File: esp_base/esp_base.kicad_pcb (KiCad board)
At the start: 2 copper layers, 35.5 x 45 mm, 52 parts, among them J1 Conn_01x02_Pin, J2 Conn_01x02_Pin, J3 Conn_01x02_Pin, U1 ESP32-C3-WROOM-02, U2 AP2112K-3.3

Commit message: added ground
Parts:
- added ?: , , F.Cu at (79.3, 91.0)
- added ?: , , F.Cu at (76.8, 91.0)
- added ?: , , F.Cu at (74.3, 91.0)
- added ?: , , F.Cu at (81.8, 91.0)
- added ?: , , F.Cu at (84.3, 91.0)
- renumbered 5V1 to 5V, GND1 to GND
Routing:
- net +3V3_UP: track 130.9 -> 134.9 mm
- net /F6: track 47.6 -> 50.7 mm
- net /F12: track 49.2 -> 49.9 mm
- net GND: vias 76 -> 75
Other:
- board text added: "GND"

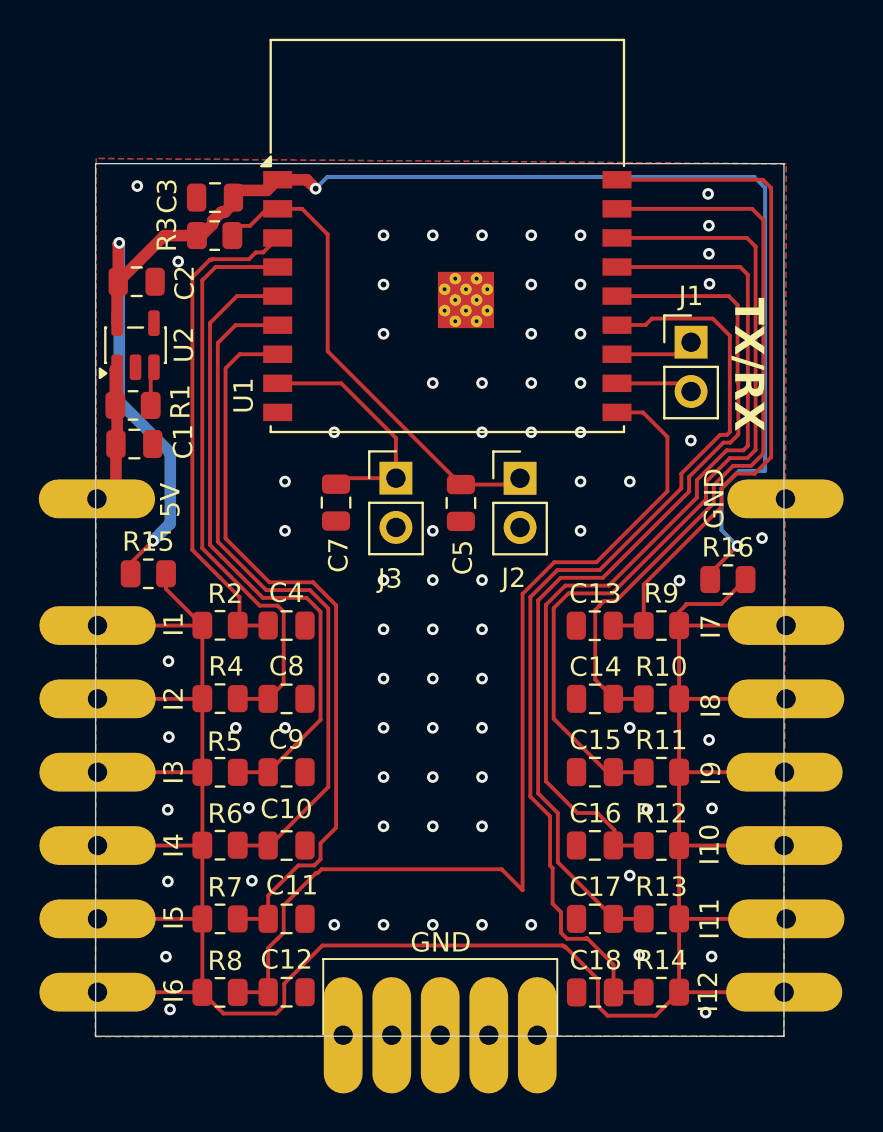
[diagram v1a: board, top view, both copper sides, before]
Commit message: komponent moved to new position smaller eddition
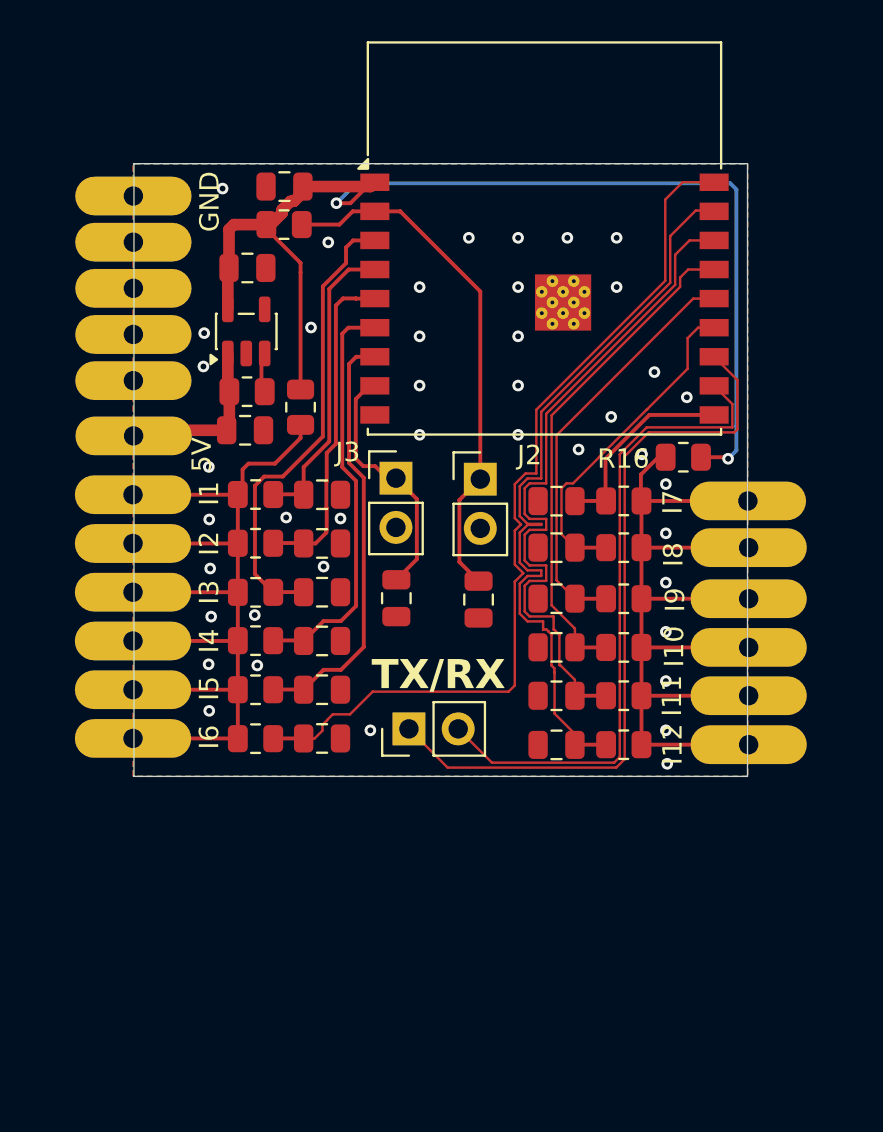
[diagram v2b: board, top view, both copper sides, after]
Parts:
- removed the ? at (79.3, 91.0)
- removed the ? at (76.8, 91.0)
- removed the ? at (74.3, 91.0)
- removed the ? at (81.8, 91.0)
- removed the ? at (84.3, 91.0)
- added ?: , , F.Cu at (63.5, 57.2)
- added ?: , , F.Cu at (63.5, 54.8)
- added ?: , , F.Cu at (63.5, 52.4)
- added ?: , , F.Cu at (63.5, 50.0)
- moved GND1 37.1 mm to (63.5, 47.7)
- moved J1 24.7 mm to (77.7, 75.2), turned to 90 degrees
- moved C12 13.2 mm to (73.2, 75.6)
- moved I6 13.2 mm to (63.4, 75.6)
- moved R8 13.2 mm to (69.7, 75.7)
- moved C18 12.9 mm to (85.3, 76.0)
- moved R14 12.9 mm to (88.7, 76.0)
- moved I12 12.9 mm to (95.2, 76.0)
- moved C11 12.0 mm to (73.2, 73.1)
- moved I5 12.0 mm to (63.4, 73.1)
- moved R7 12.0 mm to (69.7, 73.1)
- moved C17 11.7 mm to (85.3, 73.4)
- moved R13 11.7 mm to (88.7, 73.4)
- moved I11 11.7 mm to (95.2, 73.4)
- moved R15 11.6 mm to (72.1, 58.6), turned to -90 degrees
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- renumbered GND to GND1
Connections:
- U1 pad 10: /F6 -> /F7
- U1 pad 13: /F12 -> /F8
- U1 pad 14: /F11 -> /F9
- U1 pad 16: /F9 -> /F11
- U1 pad 17: /F8 -> /F12
- U1 pad 18: /F7 -> /F6
- U1 pad 3: /F1 -> /F3
- U1 pad 4: /F2 -> /F1
- U1 pad 5: /F3 -> /F2
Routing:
- net +3V3_UP: track 134.9 -> 92.9 mm
- net /TX: track 4.08 -> 38.4 mm
- net /RX: track 3.99 -> 33.7 mm
- net /F7: track 35.5 -> 10.3 mm
- net /F9: track 43.6 -> 21.4 mm
- net /F8: track 38.9 -> 17.1 mm
- net +3V3: track 82.6 -> 61.3 mm, vias 4 -> 2
- net /F10: track 46.1 -> 25.8 mm
- net /F5: track 38.5 -> 22.0 mm
- net /F4: track 35.9 -> 21.2 mm
- net /F2: track 29.8 -> 17.1 mm
- net /F11: track 47.0 -> 36.0 mm
- net /F12: track 49.9 -> 39.5 mm
- net /F1: track 25.8 -> 15.5 mm
- net /F3: track 33.5 -> 23.9 mm
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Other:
- board size 35.5 x 45 mm -> 31.6 x 31.6 mm

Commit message: NEW PADS
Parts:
- removed the 5V at (63.5, 60.0)
- removed the ? at (63.5, 57.2)
- removed the ? at (63.5, 54.8)
- removed the ? at (63.5, 52.4)
- removed the ? at (63.5, 50.0)
- removed GND1: TestPoint_Alt, TestPoint:TestPoint_THTPad_D2.0mm_Drill1.0mm
- added 5V: TestPoint_Alt, TestPoint:TestPoint_Pad_2.0x2.0mm, F.Cu at (64.8, 59.8)
- added ?: , , F.Cu at (65.3, 50.0)
- added ?: , , F.Cu at (65.3, 57.1)
- added ?: , , F.Cu at (65.3, 52.4)
- added GND: TestPoint_Alt, TestPoint:TestPoint_Pad_2.0x2.0mm, F.Cu at (65.3, 47.6)
- added GND: TestPoint_Alt, TestPoint:TestPoint_Pad_2.0x2.0mm, F.Cu at (65.3, 54.7)
- I1, I10, I11, I12, I2, I3, I4, I5, I6, I7, I8, I9: footprint TestPoint:TestPoint_THTPad_D2.0mm_Drill1.0mm -> TestPoint:TestPoint_Pad_2.0x2.0mm
- moved I7 12.8 mm to (92.7, 76.0), turned to 0 degrees
- moved I12 12.7 mm to (93.2, 63.4), turned to 0 degrees
- moved I8 7.90 mm to (93.2, 73.5), turned to 0 degrees
- moved I11 7.78 mm to (93.2, 65.9), turned to 0 degrees
- moved I10 3.35 mm to (93.2, 68.2), turned to 0 degrees
- moved I9 3.15 mm to (93.2, 70.9), turned to 0 degrees
- moved I5 1.84 mm to (65.3, 73.3), turned to 0 degrees
- moved I1 1.83 mm to (65.3, 63.0), turned to 0 degrees
- moved I4 1.83 mm to (65.3, 70.7), turned to 0 degrees
- moved I2 1.83 mm to (65.3, 65.5), turned to 0 degrees
- moved I6 1.83 mm to (65.3, 75.7), turned to 0 degrees
- moved I3 1.83 mm to (65.3, 68.1), turned to 0 degrees
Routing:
- net GND: vias 42 -> 40

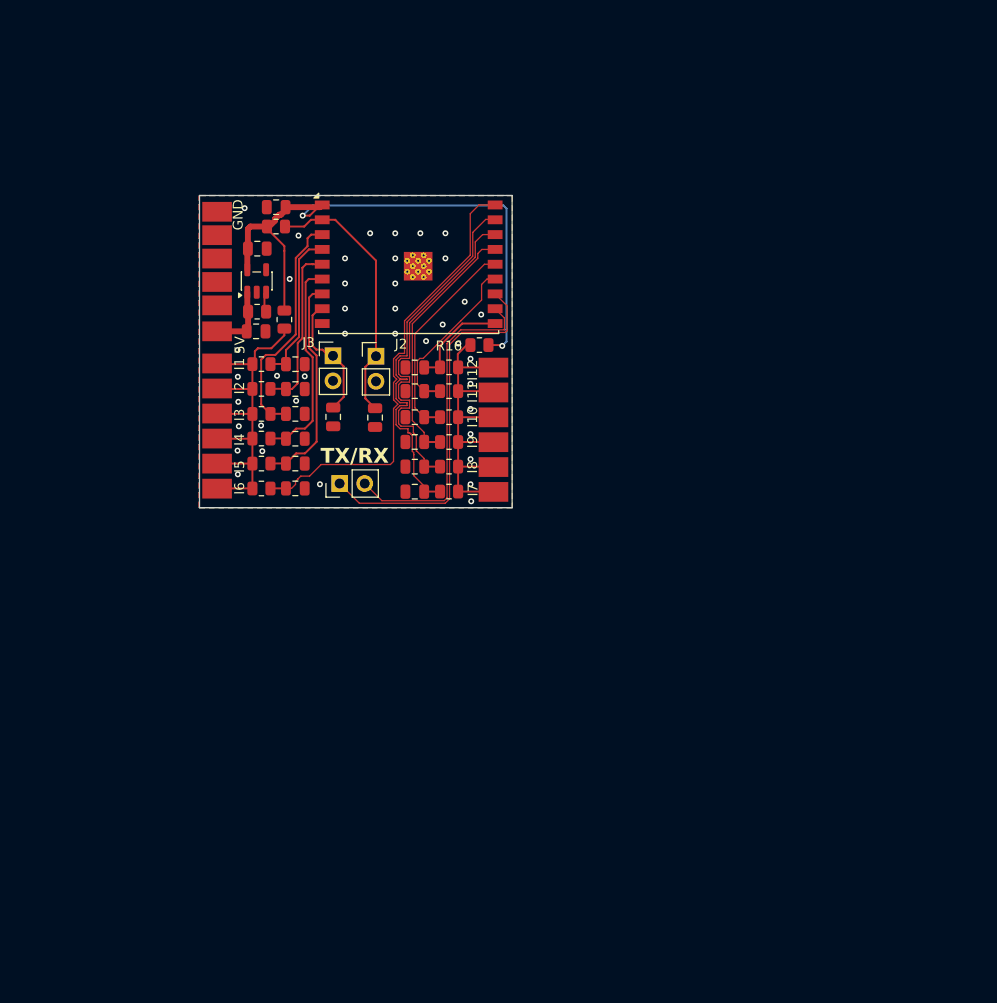
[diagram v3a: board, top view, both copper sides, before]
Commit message: last version with cahges on pull up resistor
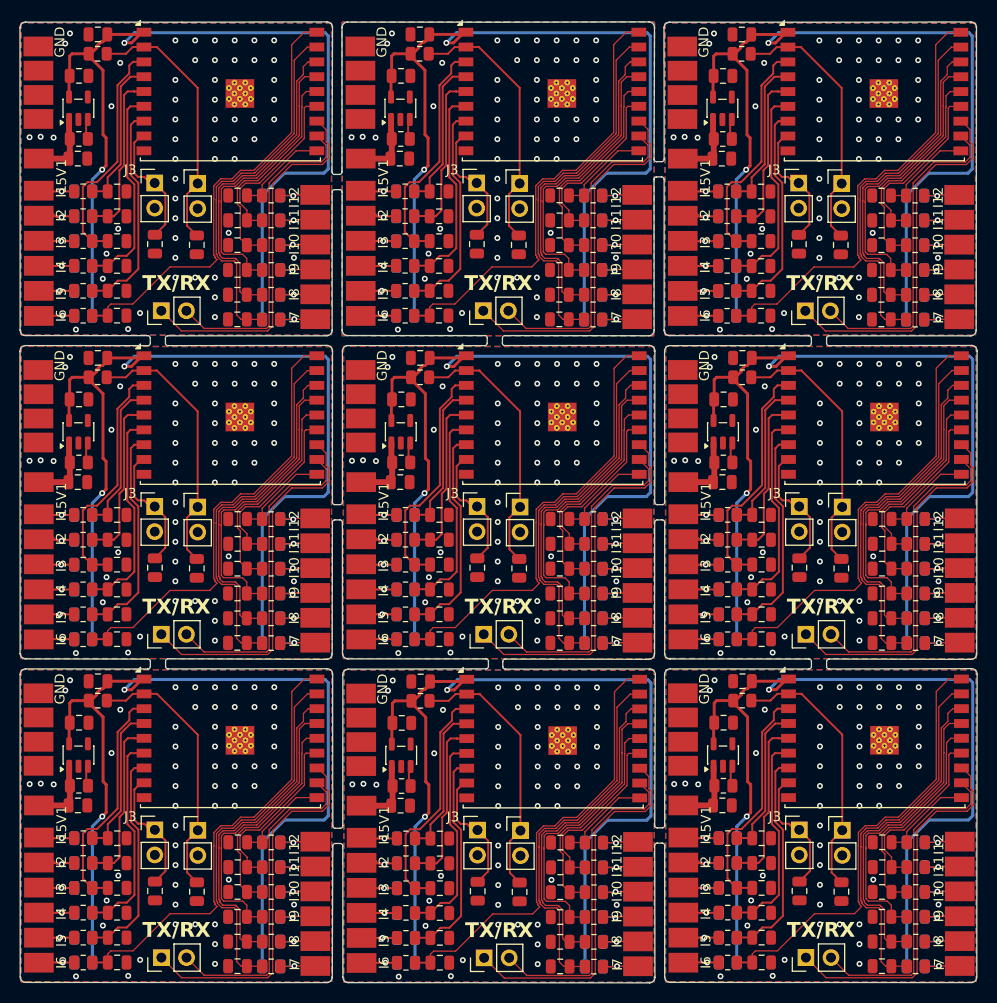
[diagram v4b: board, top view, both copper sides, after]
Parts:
- removed the ? at (65.3, 50.0)
- removed the ? at (65.3, 57.1)
- removed the ? at (65.3, 52.4)
- removed GND: TestPoint_Alt, TestPoint:TestPoint_Pad_2.0x2.0mm
- removed R15, R16: 4k7, Resistor_SMD:R_0805_2012Metric
- added 5V1: TestPoint_Alt, TestPoint:TestPoint_Pad_2.0x2.0mm, F.Cu at (111.9, 42.3)
- added 5V1: TestPoint_Alt, TestPoint:TestPoint_Pad_2.0x2.0mm, F.Cu at (111.9, 75.0)
- added 5V1: TestPoint_Alt, TestPoint:TestPoint_Pad_2.0x2.0mm, F.Cu at (79.3, 42.3)
- added 5V1: TestPoint_Alt, TestPoint:TestPoint_Pad_2.0x2.0mm, F.Cu at (46.7, 107.7)
- added 5V1: TestPoint_Alt, TestPoint:TestPoint_Pad_2.0x2.0mm, F.Cu at (46.7, 75.0)
- added 5V1: TestPoint_Alt, TestPoint:TestPoint_Pad_2.0x2.0mm, F.Cu at (112.0, 107.7)
- added 5V1: TestPoint_Alt, TestPoint:TestPoint_Pad_2.0x2.0mm, F.Cu at (79.3, 75.0)
- added 5V1: TestPoint_Alt, TestPoint:TestPoint_Pad_2.0x2.0mm, F.Cu at (79.4, 107.8)
- added ?: , , F.Cu at (112.4, 71.0)
- added ?: , , F.Cu at (79.8, 38.3)
- added ?: , , F.Cu at (79.8, 35.8)
- added ?: , , F.Cu at (79.8, 71.0)
- added ?: , , F.Cu at (47.2, 66.1)
- added ?: , , F.Cu at (112.4, 101.3)
- added ?: , , F.Cu at (47.2, 38.3)
- added ?: , , F.Cu at (79.9, 98.9)
- added ?: , , F.Cu at (79.9, 101.3)
- added ?: , , F.Cu at (47.2, 33.4)
- added ?: , , F.Cu at (79.8, 68.6)
- added ?: , , F.Cu at (112.4, 38.3)
- added ?: , , F.Cu at (112.4, 66.1)
- added ?: , , F.Cu at (47.2, 101.3)
- added ?: , , F.Cu at (79.9, 103.7)
- added ?: , , F.Cu at (47.2, 68.6)
- added ?: , , F.Cu at (112.4, 68.6)
- added ?: , , F.Cu at (112.4, 98.8)
- added ?: , , F.Cu at (79.8, 33.4)
- added ?: , , F.Cu at (79.8, 66.1)
- added ?: , , F.Cu at (112.4, 103.7)
- added ?: , , F.Cu at (112.4, 33.4)
- added ?: , , F.Cu at (47.2, 103.7)
- added ?: , , F.Cu at (47.2, 35.8)
- added ?: , , F.Cu at (47.2, 71.0)
- added ?: , , F.Cu at (47.2, 98.8)
- added ?: , , F.Cu at (112.4, 35.8)
- added C1: 1u, Capacitor_SMD:C_0805_2012Metric, F.Cu at (116.4, 75.0)
- added C1: 1u, Capacitor_SMD:C_0805_2012Metric, F.Cu at (51.2, 107.7)
- added C1: 1u, Capacitor_SMD:C_0805_2012Metric, F.Cu at (116.3, 42.3)
- added C1: 1u, Capacitor_SMD:C_0805_2012Metric, F.Cu at (83.8, 42.3)
- added C1: 1u, Capacitor_SMD:C_0805_2012Metric, F.Cu at (116.4, 107.7)
- added C1: 1u, Capacitor_SMD:C_0805_2012Metric, F.Cu at (51.2, 75.0)
- added C1: 1u, Capacitor_SMD:C_0805_2012Metric, F.Cu at (83.8, 107.8)
- added C1: 1u, Capacitor_SMD:C_0805_2012Metric, F.Cu at (83.8, 75.0)
- added C10: 4u7, Capacitor_SMD:C_0805_2012Metric, F.Cu at (87.7, 53.1)
- added C10: 4u7, Capacitor_SMD:C_0805_2012Metric, F.Cu at (120.4, 85.9)
- added C10: 4u7, Capacitor_SMD:C_0805_2012Metric, F.Cu at (87.8, 85.9)
- added C10: 4u7, Capacitor_SMD:C_0805_2012Metric, F.Cu at (87.8, 118.6)
- added C10: 4u7, Capacitor_SMD:C_0805_2012Metric, F.Cu at (120.3, 53.1)
- added C10: 4u7, Capacitor_SMD:C_0805_2012Metric, F.Cu at (55.1, 118.6)
- added C10: 4u7, Capacitor_SMD:C_0805_2012Metric, F.Cu at (55.1, 85.9)
- added C10: 4u7, Capacitor_SMD:C_0805_2012Metric, F.Cu at (120.4, 118.6)
- added C11: 4u7, Capacitor_SMD:C_0805_2012Metric, F.Cu at (120.3, 55.7)
- added C11: 4u7, Capacitor_SMD:C_0805_2012Metric, F.Cu at (87.8, 121.1)
- added C11: 4u7, Capacitor_SMD:C_0805_2012Metric, F.Cu at (120.4, 121.1)
- added C11: 4u7, Capacitor_SMD:C_0805_2012Metric, F.Cu at (87.8, 88.4)
- added C11: 4u7, Capacitor_SMD:C_0805_2012Metric, F.Cu at (120.4, 88.4)
- added C11: 4u7, Capacitor_SMD:C_0805_2012Metric, F.Cu at (55.1, 121.1)
- added C11: 4u7, Capacitor_SMD:C_0805_2012Metric, F.Cu at (87.7, 55.6)
- added C11: 4u7, Capacitor_SMD:C_0805_2012Metric, F.Cu at (55.1, 88.4)
- added C12: 4u7, Capacitor_SMD:C_0805_2012Metric, F.Cu at (55.1, 123.6)
- added C12: 4u7, Capacitor_SMD:C_0805_2012Metric, F.Cu at (87.8, 90.9)
- added C12: 4u7, Capacitor_SMD:C_0805_2012Metric, F.Cu at (87.7, 58.2)
- added C12: 4u7, Capacitor_SMD:C_0805_2012Metric, F.Cu at (120.3, 58.2)
- added C12: 4u7, Capacitor_SMD:C_0805_2012Metric, F.Cu at (120.4, 90.9)
- added C12: 4u7, Capacitor_SMD:C_0805_2012Metric, F.Cu at (87.8, 123.6)
- added C12: 4u7, Capacitor_SMD:C_0805_2012Metric, F.Cu at (55.1, 90.9)
- added C12: 4u7, Capacitor_SMD:C_0805_2012Metric, F.Cu at (120.4, 123.6)
- added C13: 4u7, Capacitor_SMD:C_0805_2012Metric, F.Cu at (132.5, 124.0)
- added C13: 4u7, Capacitor_SMD:C_0805_2012Metric, F.Cu at (100.0, 124.0)
- added C13: 4u7, Capacitor_SMD:C_0805_2012Metric, F.Cu at (99.9, 91.3)
- added C13: 4u7, Capacitor_SMD:C_0805_2012Metric, F.Cu at (67.3, 124.0)
- added C13: 4u7, Capacitor_SMD:C_0805_2012Metric, F.Cu at (132.5, 91.3)
- added C13: 4u7, Capacitor_SMD:C_0805_2012Metric, F.Cu at (99.9, 58.5)
- added C13: 4u7, Capacitor_SMD:C_0805_2012Metric, F.Cu at (67.3, 91.3)
- added C13: 4u7, Capacitor_SMD:C_0805_2012Metric, F.Cu at (132.5, 58.5)
- added C14: 4u7, Capacitor_SMD:C_0805_2012Metric, F.Cu at (67.3, 121.5)
- added C14: 4u7, Capacitor_SMD:C_0805_2012Metric, F.Cu at (132.5, 56.1)
- added C14: 4u7, Capacitor_SMD:C_0805_2012Metric, F.Cu at (99.9, 56.0)
- added C14: 4u7, Capacitor_SMD:C_0805_2012Metric, F.Cu at (132.5, 121.5)
- added C14: 4u7, Capacitor_SMD:C_0805_2012Metric, F.Cu at (99.9, 88.8)
- added C14: 4u7, Capacitor_SMD:C_0805_2012Metric, F.Cu at (67.3, 88.8)
- added C14: 4u7, Capacitor_SMD:C_0805_2012Metric, F.Cu at (100.0, 121.5)
- added C14: 4u7, Capacitor_SMD:C_0805_2012Metric, F.Cu at (132.5, 88.8)
- added C15: 4u7, Capacitor_SMD:C_0805_2012Metric, F.Cu at (100.0, 119.0)
- added C15: 4u7, Capacitor_SMD:C_0805_2012Metric, F.Cu at (67.3, 86.3)
- added C15: 4u7, Capacitor_SMD:C_0805_2012Metric, F.Cu at (132.5, 86.3)
- added C15: 4u7, Capacitor_SMD:C_0805_2012Metric, F.Cu at (99.9, 86.3)
- added C15: 4u7, Capacitor_SMD:C_0805_2012Metric, F.Cu at (67.3, 119.0)
- added C15: 4u7, Capacitor_SMD:C_0805_2012Metric, F.Cu at (99.9, 53.5)
- added C15: 4u7, Capacitor_SMD:C_0805_2012Metric, F.Cu at (132.5, 119.0)
- added C15: 4u7, Capacitor_SMD:C_0805_2012Metric, F.Cu at (132.5, 53.5)
- added C16: 4u7, Capacitor_SMD:C_0805_2012Metric, F.Cu at (100.0, 83.8)
- added C16: 4u7, Capacitor_SMD:C_0805_2012Metric, F.Cu at (67.3, 116.5)
- added C16: 4u7, Capacitor_SMD:C_0805_2012Metric, F.Cu at (100.0, 116.5)
- added C16: 4u7, Capacitor_SMD:C_0805_2012Metric, F.Cu at (99.9, 51.0)
- added C16: 4u7, Capacitor_SMD:C_0805_2012Metric, F.Cu at (132.5, 51.0)
- added C16: 4u7, Capacitor_SMD:C_0805_2012Metric, F.Cu at (132.6, 83.8)
- added C16: 4u7, Capacitor_SMD:C_0805_2012Metric, F.Cu at (67.3, 83.8)
- added C16: 4u7, Capacitor_SMD:C_0805_2012Metric, F.Cu at (132.6, 116.5)
- added C17: 4u7, Capacitor_SMD:C_0805_2012Metric, F.Cu at (132.5, 48.5)
- added C17: 4u7, Capacitor_SMD:C_0805_2012Metric, F.Cu at (132.6, 114.0)
- added C17: 4u7, Capacitor_SMD:C_0805_2012Metric, F.Cu at (99.9, 48.5)
- added C17: 4u7, Capacitor_SMD:C_0805_2012Metric, F.Cu at (100.0, 81.3)
- added C17: 4u7, Capacitor_SMD:C_0805_2012Metric, F.Cu at (100.0, 114.0)
- added C17: 4u7, Capacitor_SMD:C_0805_2012Metric, F.Cu at (67.3, 114.0)
- added C17: 4u7, Capacitor_SMD:C_0805_2012Metric, F.Cu at (67.3, 81.3)
- added C17: 4u7, Capacitor_SMD:C_0805_2012Metric, F.Cu at (132.6, 81.3)
- added C18: 4u7, Capacitor_SMD:C_0805_2012Metric, F.Cu at (132.6, 111.5)
- added C18: 4u7, Capacitor_SMD:C_0805_2012Metric, F.Cu at (132.6, 78.7)
- added C18: 4u7, Capacitor_SMD:C_0805_2012Metric, F.Cu at (67.3, 78.7)
- added C18: 4u7, Capacitor_SMD:C_0805_2012Metric, F.Cu at (132.5, 46.0)
- added C18: 4u7, Capacitor_SMD:C_0805_2012Metric, F.Cu at (100.0, 78.7)
- added C18: 4u7, Capacitor_SMD:C_0805_2012Metric, F.Cu at (99.9, 46.0)
- added C18: 4u7, Capacitor_SMD:C_0805_2012Metric, F.Cu at (100.0, 111.5)
- added C18: 4u7, Capacitor_SMD:C_0805_2012Metric, F.Cu at (67.3, 111.5)
- added C2: 1u, Capacitor_SMD:C_0805_2012Metric, F.Cu at (116.5, 99.4)
- added C2: 1u, Capacitor_SMD:C_0805_2012Metric, F.Cu at (84.0, 99.4)
- added C2: 1u, Capacitor_SMD:C_0805_2012Metric, F.Cu at (116.5, 33.9)
- added C2: 1u, Capacitor_SMD:C_0805_2012Metric, F.Cu at (83.9, 33.9)
- added C2: 1u, Capacitor_SMD:C_0805_2012Metric, F.Cu at (116.5, 66.6)
- added C2: 1u, Capacitor_SMD:C_0805_2012Metric, F.Cu at (83.9, 66.6)
- added C2: 1u, Capacitor_SMD:C_0805_2012Metric, F.Cu at (51.3, 66.6)
- added C2: 1u, Capacitor_SMD:C_0805_2012Metric, F.Cu at (51.3, 99.4)
- added C3: 1u, Capacitor_SMD:C_0805_2012Metric, F.Cu at (118.4, 29.7)
- added C3: 1u, Capacitor_SMD:C_0805_2012Metric, F.Cu at (53.2, 95.2)
- added C3: 1u, Capacitor_SMD:C_0805_2012Metric, F.Cu at (85.9, 95.2)
- added C3: 1u, Capacitor_SMD:C_0805_2012Metric, F.Cu at (85.8, 29.7)
- added C3: 1u, Capacitor_SMD:C_0805_2012Metric, F.Cu at (85.8, 62.4)
- added C3: 1u, Capacitor_SMD:C_0805_2012Metric, F.Cu at (118.4, 62.4)
- added C3: 1u, Capacitor_SMD:C_0805_2012Metric, F.Cu at (118.4, 95.2)
- added C3: 1u, Capacitor_SMD:C_0805_2012Metric, F.Cu at (53.2, 62.4)
- added C4: 4u7, Capacitor_SMD:C_0805_2012Metric, F.Cu at (87.8, 78.3)
- added C4: 4u7, Capacitor_SMD:C_0805_2012Metric, F.Cu at (55.1, 78.3)
- added C4: 4u7, Capacitor_SMD:C_0805_2012Metric, F.Cu at (55.1, 111.1)
- added C4: 4u7, Capacitor_SMD:C_0805_2012Metric, F.Cu at (120.4, 111.0)
- added C4: 4u7, Capacitor_SMD:C_0805_2012Metric, F.Cu at (87.8, 111.1)
- added C4: 4u7, Capacitor_SMD:C_0805_2012Metric, F.Cu at (120.4, 78.3)
- added C4: 4u7, Capacitor_SMD:C_0805_2012Metric, F.Cu at (120.3, 45.6)
- added C4: 4u7, Capacitor_SMD:C_0805_2012Metric, F.Cu at (87.7, 45.6)
- added C5: 1u, Capacitor_SMD:C_0805_2012Metric, F.Cu at (95.9, 116.5)
- added C5: 1u, Capacitor_SMD:C_0805_2012Metric, F.Cu at (63.2, 83.7)
- added C5: 1u, Capacitor_SMD:C_0805_2012Metric, F.Cu at (128.4, 83.7)
- added C5: 1u, Capacitor_SMD:C_0805_2012Metric, F.Cu at (63.2, 116.5)
- added C5: 1u, Capacitor_SMD:C_0805_2012Metric, F.Cu at (95.8, 83.7)
- added C5: 1u, Capacitor_SMD:C_0805_2012Metric, F.Cu at (128.4, 116.5)
- added C5: 1u, Capacitor_SMD:C_0805_2012Metric, F.Cu at (128.4, 51.0)
- added C5: 1u, Capacitor_SMD:C_0805_2012Metric, F.Cu at (95.8, 51.0)
- added C7: 1u, Capacitor_SMD:C_0805_2012Metric, F.Cu at (124.1, 50.9)
- added C7: 1u, Capacitor_SMD:C_0805_2012Metric, F.Cu at (124.2, 116.4)
- added C7: 1u, Capacitor_SMD:C_0805_2012Metric, F.Cu at (59.0, 116.4)
- added C7: 1u, Capacitor_SMD:C_0805_2012Metric, F.Cu at (59.0, 83.7)
- added C7: 1u, Capacitor_SMD:C_0805_2012Metric, F.Cu at (91.6, 116.4)
- added C7: 1u, Capacitor_SMD:C_0805_2012Metric, F.Cu at (91.6, 83.7)
- added C7: 1u, Capacitor_SMD:C_0805_2012Metric, F.Cu at (91.6, 50.9)
- added C7: 1u, Capacitor_SMD:C_0805_2012Metric, F.Cu at (124.2, 83.7)
- added C8: 4u7, Capacitor_SMD:C_0805_2012Metric, F.Cu at (55.1, 80.8)
- added C8: 4u7, Capacitor_SMD:C_0805_2012Metric, F.Cu at (87.7, 48.1)
- added C8: 4u7, Capacitor_SMD:C_0805_2012Metric, F.Cu at (87.8, 113.6)
- added C8: 4u7, Capacitor_SMD:C_0805_2012Metric, F.Cu at (120.4, 113.6)
- added C8: 4u7, Capacitor_SMD:C_0805_2012Metric, F.Cu at (55.1, 113.6)
- added C8: 4u7, Capacitor_SMD:C_0805_2012Metric, F.Cu at (120.3, 48.1)
- added C8: 4u7, Capacitor_SMD:C_0805_2012Metric, F.Cu at (87.8, 80.8)
- added C8: 4u7, Capacitor_SMD:C_0805_2012Metric, F.Cu at (120.4, 80.8)
- added C9: 4u7, Capacitor_SMD:C_0805_2012Metric, F.Cu at (120.3, 50.6)
- added C9: 4u7, Capacitor_SMD:C_0805_2012Metric, F.Cu at (55.1, 83.4)
- added C9: 4u7, Capacitor_SMD:C_0805_2012Metric, F.Cu at (87.7, 50.6)
- added C9: 4u7, Capacitor_SMD:C_0805_2012Metric, F.Cu at (120.4, 116.1)
- added C9: 4u7, Capacitor_SMD:C_0805_2012Metric, F.Cu at (87.8, 116.1)
- added C9: 4u7, Capacitor_SMD:C_0805_2012Metric, F.Cu at (120.4, 83.4)
- added C9: 4u7, Capacitor_SMD:C_0805_2012Metric, F.Cu at (87.8, 83.4)
- added C9: 4u7, Capacitor_SMD:C_0805_2012Metric, F.Cu at (55.1, 116.1)
- added GND1: TestPoint_Alt, TestPoint:TestPoint_Pad_2.0x2.0mm, F.Cu at (112.4, 63.7)
- added GND1: TestPoint_Alt, TestPoint:TestPoint_Pad_2.0x2.0mm, F.Cu at (47.2, 96.4)
- added GND1: TestPoint_Alt, TestPoint:TestPoint_Pad_2.0x2.0mm, F.Cu at (47.2, 63.7)
- added GND1: TestPoint_Alt, TestPoint:TestPoint_Pad_2.0x2.0mm, F.Cu at (112.3, 30.9)
- added GND1: TestPoint_Alt, TestPoint:TestPoint_Pad_2.0x2.0mm, F.Cu at (79.8, 63.7)
- added GND1: TestPoint_Alt, TestPoint:TestPoint_Pad_2.0x2.0mm, F.Cu at (112.4, 96.4)
- added GND1: TestPoint_Alt, TestPoint:TestPoint_Pad_2.0x2.0mm, F.Cu at (79.7, 30.9)
- added GND1: TestPoint_Alt, TestPoint:TestPoint_Pad_2.0x2.0mm, F.Cu at (79.8, 96.4)
- added I1: TestPoint_Alt, TestPoint:TestPoint_Pad_2.0x2.0mm, F.Cu at (79.8, 45.5)
- added I1: TestPoint_Alt, TestPoint:TestPoint_Pad_2.0x2.0mm, F.Cu at (112.4, 45.5)
- added I1: TestPoint_Alt, TestPoint:TestPoint_Pad_2.0x2.0mm, F.Cu at (112.5, 111.0)
- added I1: TestPoint_Alt, TestPoint:TestPoint_Pad_2.0x2.0mm, F.Cu at (112.4, 78.3)
- added I1: TestPoint_Alt, TestPoint:TestPoint_Pad_2.0x2.0mm, F.Cu at (79.9, 111.0)
- added I1: TestPoint_Alt, TestPoint:TestPoint_Pad_2.0x2.0mm, F.Cu at (47.2, 78.3)
- added I1: TestPoint_Alt, TestPoint:TestPoint_Pad_2.0x2.0mm, F.Cu at (79.8, 78.3)
- added I1: TestPoint_Alt, TestPoint:TestPoint_Pad_2.0x2.0mm, F.Cu at (47.2, 111.0)
- added I10: TestPoint_Alt, TestPoint:TestPoint_Pad_2.0x2.0mm, F.Cu at (107.8, 50.7)
- added I10: TestPoint_Alt, TestPoint:TestPoint_Pad_2.0x2.0mm, F.Cu at (107.9, 116.2)
- added I10: TestPoint_Alt, TestPoint:TestPoint_Pad_2.0x2.0mm, F.Cu at (107.8, 83.5)
- added I10: TestPoint_Alt, TestPoint:TestPoint_Pad_2.0x2.0mm, F.Cu at (140.4, 83.5)
- added I10: TestPoint_Alt, TestPoint:TestPoint_Pad_2.0x2.0mm, F.Cu at (140.4, 116.2)
- added I10: TestPoint_Alt, TestPoint:TestPoint_Pad_2.0x2.0mm, F.Cu at (140.4, 50.7)
- added I10: TestPoint_Alt, TestPoint:TestPoint_Pad_2.0x2.0mm, F.Cu at (75.2, 83.5)
- added I10: TestPoint_Alt, TestPoint:TestPoint_Pad_2.0x2.0mm, F.Cu at (75.2, 116.2)
- added I11: TestPoint_Alt, TestPoint:TestPoint_Pad_2.0x2.0mm, F.Cu at (107.8, 81.2)
- added I11: TestPoint_Alt, TestPoint:TestPoint_Pad_2.0x2.0mm, F.Cu at (140.4, 81.2)
- added I11: TestPoint_Alt, TestPoint:TestPoint_Pad_2.0x2.0mm, F.Cu at (107.9, 113.9)
- added I11: TestPoint_Alt, TestPoint:TestPoint_Pad_2.0x2.0mm, F.Cu at (107.8, 48.4)
- added I11: TestPoint_Alt, TestPoint:TestPoint_Pad_2.0x2.0mm, F.Cu at (75.2, 81.2)
- added I11: TestPoint_Alt, TestPoint:TestPoint_Pad_2.0x2.0mm, F.Cu at (140.4, 113.9)
- added I11: TestPoint_Alt, TestPoint:TestPoint_Pad_2.0x2.0mm, F.Cu at (75.2, 113.9)
- added I11: TestPoint_Alt, TestPoint:TestPoint_Pad_2.0x2.0mm, F.Cu at (140.4, 48.4)
- added I12: TestPoint_Alt, TestPoint:TestPoint_Pad_2.0x2.0mm, F.Cu at (107.8, 78.7)
- added I12: TestPoint_Alt, TestPoint:TestPoint_Pad_2.0x2.0mm, F.Cu at (75.2, 78.7)
- added I12: TestPoint_Alt, TestPoint:TestPoint_Pad_2.0x2.0mm, F.Cu at (140.4, 111.4)
- added I12: TestPoint_Alt, TestPoint:TestPoint_Pad_2.0x2.0mm, F.Cu at (140.4, 45.9)
- added I12: TestPoint_Alt, TestPoint:TestPoint_Pad_2.0x2.0mm, F.Cu at (107.9, 111.4)
- added I12: TestPoint_Alt, TestPoint:TestPoint_Pad_2.0x2.0mm, F.Cu at (107.8, 45.9)
- added I12: TestPoint_Alt, TestPoint:TestPoint_Pad_2.0x2.0mm, F.Cu at (140.4, 78.7)
- added I12: TestPoint_Alt, TestPoint:TestPoint_Pad_2.0x2.0mm, F.Cu at (75.2, 111.4)
- added I2: TestPoint_Alt, TestPoint:TestPoint_Pad_2.0x2.0mm, F.Cu at (112.4, 80.8)
- added I2: TestPoint_Alt, TestPoint:TestPoint_Pad_2.0x2.0mm, F.Cu at (47.2, 80.8)
- added I2: TestPoint_Alt, TestPoint:TestPoint_Pad_2.0x2.0mm, F.Cu at (112.4, 48.1)
- added I2: TestPoint_Alt, TestPoint:TestPoint_Pad_2.0x2.0mm, F.Cu at (79.8, 80.8)
- added I2: TestPoint_Alt, TestPoint:TestPoint_Pad_2.0x2.0mm, F.Cu at (79.9, 113.6)
- added I2: TestPoint_Alt, TestPoint:TestPoint_Pad_2.0x2.0mm, F.Cu at (47.2, 113.5)
- added I2: TestPoint_Alt, TestPoint:TestPoint_Pad_2.0x2.0mm, F.Cu at (112.5, 113.5)
- added I2: TestPoint_Alt, TestPoint:TestPoint_Pad_2.0x2.0mm, F.Cu at (79.8, 48.1)
- added I3: TestPoint_Alt, TestPoint:TestPoint_Pad_2.0x2.0mm, F.Cu at (79.8, 50.6)
- added I3: TestPoint_Alt, TestPoint:TestPoint_Pad_2.0x2.0mm, F.Cu at (112.4, 50.6)
- added I3: TestPoint_Alt, TestPoint:TestPoint_Pad_2.0x2.0mm, F.Cu at (112.4, 83.4)
- added I3: TestPoint_Alt, TestPoint:TestPoint_Pad_2.0x2.0mm, F.Cu at (112.5, 116.1)
- added I3: TestPoint_Alt, TestPoint:TestPoint_Pad_2.0x2.0mm, F.Cu at (79.8, 83.4)
- added I3: TestPoint_Alt, TestPoint:TestPoint_Pad_2.0x2.0mm, F.Cu at (47.2, 83.4)
- added I3: TestPoint_Alt, TestPoint:TestPoint_Pad_2.0x2.0mm, F.Cu at (47.2, 116.1)
- added I3: TestPoint_Alt, TestPoint:TestPoint_Pad_2.0x2.0mm, F.Cu at (79.9, 116.1)
- added I4: TestPoint_Alt, TestPoint:TestPoint_Pad_2.0x2.0mm, F.Cu at (79.8, 53.2)
- added I4: TestPoint_Alt, TestPoint:TestPoint_Pad_2.0x2.0mm, F.Cu at (47.2, 85.9)
- added I4: TestPoint_Alt, TestPoint:TestPoint_Pad_2.0x2.0mm, F.Cu at (112.4, 53.2)
- added I4: TestPoint_Alt, TestPoint:TestPoint_Pad_2.0x2.0mm, F.Cu at (112.4, 85.9)
- added I4: TestPoint_Alt, TestPoint:TestPoint_Pad_2.0x2.0mm, F.Cu at (79.8, 85.9)
- added I4: TestPoint_Alt, TestPoint:TestPoint_Pad_2.0x2.0mm, F.Cu at (47.2, 118.6)
- added I4: TestPoint_Alt, TestPoint:TestPoint_Pad_2.0x2.0mm, F.Cu at (112.5, 118.6)
- added I4: TestPoint_Alt, TestPoint:TestPoint_Pad_2.0x2.0mm, F.Cu at (79.9, 118.7)
- added I5: TestPoint_Alt, TestPoint:TestPoint_Pad_2.0x2.0mm, F.Cu at (112.4, 88.6)
- added I5: TestPoint_Alt, TestPoint:TestPoint_Pad_2.0x2.0mm, F.Cu at (112.5, 121.3)
- added I5: TestPoint_Alt, TestPoint:TestPoint_Pad_2.0x2.0mm, F.Cu at (47.2, 121.3)
- added I5: TestPoint_Alt, TestPoint:TestPoint_Pad_2.0x2.0mm, F.Cu at (79.9, 121.4)
- added I5: TestPoint_Alt, TestPoint:TestPoint_Pad_2.0x2.0mm, F.Cu at (79.8, 88.6)
- added I5: TestPoint_Alt, TestPoint:TestPoint_Pad_2.0x2.0mm, F.Cu at (47.2, 88.6)
- added I5: TestPoint_Alt, TestPoint:TestPoint_Pad_2.0x2.0mm, F.Cu at (79.8, 55.9)
- added I5: TestPoint_Alt, TestPoint:TestPoint_Pad_2.0x2.0mm, F.Cu at (112.4, 55.9)
- added I6: TestPoint_Alt, TestPoint:TestPoint_Pad_2.0x2.0mm, F.Cu at (47.2, 90.9)
- added I6: TestPoint_Alt, TestPoint:TestPoint_Pad_2.0x2.0mm, F.Cu at (112.5, 123.6)
- added I6: TestPoint_Alt, TestPoint:TestPoint_Pad_2.0x2.0mm, F.Cu at (79.9, 123.7)
- added I6: TestPoint_Alt, TestPoint:TestPoint_Pad_2.0x2.0mm, F.Cu at (112.4, 58.2)
- added I6: TestPoint_Alt, TestPoint:TestPoint_Pad_2.0x2.0mm, F.Cu at (47.2, 123.6)
- added I6: TestPoint_Alt, TestPoint:TestPoint_Pad_2.0x2.0mm, F.Cu at (79.8, 58.2)
- added I6: TestPoint_Alt, TestPoint:TestPoint_Pad_2.0x2.0mm, F.Cu at (79.8, 90.9)
- added I6: TestPoint_Alt, TestPoint:TestPoint_Pad_2.0x2.0mm, F.Cu at (112.4, 90.9)
- added I7: TestPoint_Alt, TestPoint:TestPoint_Pad_2.0x2.0mm, F.Cu at (107.4, 124.0)
- added I7: TestPoint_Alt, TestPoint:TestPoint_Pad_2.0x2.0mm, F.Cu at (74.7, 91.3)
- added I7: TestPoint_Alt, TestPoint:TestPoint_Pad_2.0x2.0mm, F.Cu at (107.3, 58.5)
- added I7: TestPoint_Alt, TestPoint:TestPoint_Pad_2.0x2.0mm, F.Cu at (139.9, 91.3)
- added I7: TestPoint_Alt, TestPoint:TestPoint_Pad_2.0x2.0mm, F.Cu at (107.3, 91.3)
- added I7: TestPoint_Alt, TestPoint:TestPoint_Pad_2.0x2.0mm, F.Cu at (139.9, 124.0)
- added I7: TestPoint_Alt, TestPoint:TestPoint_Pad_2.0x2.0mm, F.Cu at (139.9, 58.5)
- added I7: TestPoint_Alt, TestPoint:TestPoint_Pad_2.0x2.0mm, F.Cu at (74.7, 124.0)
- added I8: TestPoint_Alt, TestPoint:TestPoint_Pad_2.0x2.0mm, F.Cu at (140.4, 88.7)
- added I8: TestPoint_Alt, TestPoint:TestPoint_Pad_2.0x2.0mm, F.Cu at (75.2, 88.7)
- added I8: TestPoint_Alt, TestPoint:TestPoint_Pad_2.0x2.0mm, F.Cu at (107.9, 121.5)
- added I8: TestPoint_Alt, TestPoint:TestPoint_Pad_2.0x2.0mm, F.Cu at (107.8, 88.7)
- added I8: TestPoint_Alt, TestPoint:TestPoint_Pad_2.0x2.0mm, F.Cu at (107.8, 56.0)
- added I8: TestPoint_Alt, TestPoint:TestPoint_Pad_2.0x2.0mm, F.Cu at (140.4, 56.0)
- added I8: TestPoint_Alt, TestPoint:TestPoint_Pad_2.0x2.0mm, F.Cu at (75.2, 121.4)
- added I8: TestPoint_Alt, TestPoint:TestPoint_Pad_2.0x2.0mm, F.Cu at (140.4, 121.4)
- added I9: TestPoint_Alt, TestPoint:TestPoint_Pad_2.0x2.0mm, F.Cu at (107.8, 53.4)
- added I9: TestPoint_Alt, TestPoint:TestPoint_Pad_2.0x2.0mm, F.Cu at (75.2, 86.2)
- added I9: TestPoint_Alt, TestPoint:TestPoint_Pad_2.0x2.0mm, F.Cu at (107.8, 86.2)
- added I9: TestPoint_Alt, TestPoint:TestPoint_Pad_2.0x2.0mm, F.Cu at (140.4, 53.4)
- added I9: TestPoint_Alt, TestPoint:TestPoint_Pad_2.0x2.0mm, F.Cu at (140.4, 86.2)
- added I9: TestPoint_Alt, TestPoint:TestPoint_Pad_2.0x2.0mm, F.Cu at (75.2, 118.9)
- added I9: TestPoint_Alt, TestPoint:TestPoint_Pad_2.0x2.0mm, F.Cu at (107.9, 118.9)
- added I9: TestPoint_Alt, TestPoint:TestPoint_Pad_2.0x2.0mm, F.Cu at (140.4, 118.9)
- added J1: Conn_01x02_Pin, Connector_PinHeader_2.54mm:PinHeader_1x02_P2.54mm_Vertical, F.Cu at (124.9, 123.1)
- added J1: Conn_01x02_Pin, Connector_PinHeader_2.54mm:PinHeader_1x02_P2.54mm_Vertical, F.Cu at (124.8, 90.4)
- added J1: Conn_01x02_Pin, Connector_PinHeader_2.54mm:PinHeader_1x02_P2.54mm_Vertical, F.Cu at (59.6, 123.1)
- added J1: Conn_01x02_Pin, Connector_PinHeader_2.54mm:PinHeader_1x02_P2.54mm_Vertical, F.Cu at (124.8, 57.7)
- added J1: Conn_01x02_Pin, Connector_PinHeader_2.54mm:PinHeader_1x02_P2.54mm_Vertical, F.Cu at (59.6, 90.4)
- added J1: Conn_01x02_Pin, Connector_PinHeader_2.54mm:PinHeader_1x02_P2.54mm_Vertical, F.Cu at (92.3, 123.2)
- added J1: Conn_01x02_Pin, Connector_PinHeader_2.54mm:PinHeader_1x02_P2.54mm_Vertical, F.Cu at (92.2, 57.7)
- added J1: Conn_01x02_Pin, Connector_PinHeader_2.54mm:PinHeader_1x02_P2.54mm_Vertical, F.Cu at (92.2, 90.4)
- added J2: Conn_01x02_Pin, Connector_PinHeader_2.54mm:PinHeader_1x02_P2.54mm_Vertical, F.Cu at (128.5, 110.2)
- added J2: Conn_01x02_Pin, Connector_PinHeader_2.54mm:PinHeader_1x02_P2.54mm_Vertical, F.Cu at (128.5, 44.8)
- added J2: Conn_01x02_Pin, Connector_PinHeader_2.54mm:PinHeader_1x02_P2.54mm_Vertical, F.Cu at (63.3, 77.5)
- added J2: Conn_01x02_Pin, Connector_PinHeader_2.54mm:PinHeader_1x02_P2.54mm_Vertical, F.Cu at (96.0, 110.3)
- added J2: Conn_01x02_Pin, Connector_PinHeader_2.54mm:PinHeader_1x02_P2.54mm_Vertical, F.Cu at (95.9, 44.8)
- added J2: Conn_01x02_Pin, Connector_PinHeader_2.54mm:PinHeader_1x02_P2.54mm_Vertical, F.Cu at (128.5, 77.5)
- added J2: Conn_01x02_Pin, Connector_PinHeader_2.54mm:PinHeader_1x02_P2.54mm_Vertical, F.Cu at (95.9, 77.5)
- added J2: Conn_01x02_Pin, Connector_PinHeader_2.54mm:PinHeader_1x02_P2.54mm_Vertical, F.Cu at (63.3, 110.2)
- added J3: Conn_01x02_Pin, Connector_PinHeader_2.54mm:PinHeader_1x02_P2.54mm_Vertical, F.Cu at (124.1, 44.7)
- added J3: Conn_01x02_Pin, Connector_PinHeader_2.54mm:PinHeader_1x02_P2.54mm_Vertical, F.Cu at (91.5, 44.7)
- added J3: Conn_01x02_Pin, Connector_PinHeader_2.54mm:PinHeader_1x02_P2.54mm_Vertical, F.Cu at (91.6, 110.2)
- added J3: Conn_01x02_Pin, Connector_PinHeader_2.54mm:PinHeader_1x02_P2.54mm_Vertical, F.Cu at (58.9, 77.5)
- added J3: Conn_01x02_Pin, Connector_PinHeader_2.54mm:PinHeader_1x02_P2.54mm_Vertical, F.Cu at (124.2, 110.2)
- added J3: Conn_01x02_Pin, Connector_PinHeader_2.54mm:PinHeader_1x02_P2.54mm_Vertical, F.Cu at (91.6, 77.5)
- added J3: Conn_01x02_Pin, Connector_PinHeader_2.54mm:PinHeader_1x02_P2.54mm_Vertical, F.Cu at (59.0, 110.2)
- added J3: Conn_01x02_Pin, Connector_PinHeader_2.54mm:PinHeader_1x02_P2.54mm_Vertical, F.Cu at (124.2, 77.5)
- added R1: 1k, Resistor_SMD:R_0805_2012Metric, F.Cu at (116.4, 40.3)
- added R1: 1k, Resistor_SMD:R_0805_2012Metric, F.Cu at (83.9, 73.0)
- added R1: 1k, Resistor_SMD:R_0805_2012Metric, F.Cu at (116.5, 105.7)
- added R1: 1k, Resistor_SMD:R_0805_2012Metric, F.Cu at (83.9, 40.3)
- added R1: 1k, Resistor_SMD:R_0805_2012Metric, F.Cu at (116.5, 73.0)
- added R1: 1k, Resistor_SMD:R_0805_2012Metric, F.Cu at (51.3, 73.0)
- added R1: 1k, Resistor_SMD:R_0805_2012Metric, F.Cu at (83.9, 105.8)
- added R1: 1k, Resistor_SMD:R_0805_2012Metric, F.Cu at (51.3, 105.7)
- added R10: 10k, Resistor_SMD:R_0805_2012Metric, F.Cu at (136.0, 88.8)
- added R10: 10k, Resistor_SMD:R_0805_2012Metric, F.Cu at (135.9, 56.1)
- added R10: 10k, Resistor_SMD:R_0805_2012Metric, F.Cu at (136.0, 121.5)
- added R10: 10k, Resistor_SMD:R_0805_2012Metric, F.Cu at (103.4, 88.8)
- added R10: 10k, Resistor_SMD:R_0805_2012Metric, F.Cu at (70.7, 121.5)
- added R10: 10k, Resistor_SMD:R_0805_2012Metric, F.Cu at (103.3, 56.0)
- added R10: 10k, Resistor_SMD:R_0805_2012Metric, F.Cu at (103.4, 121.5)
- added R10: 10k, Resistor_SMD:R_0805_2012Metric, F.Cu at (70.7, 88.8)
- added R11: 10k, Resistor_SMD:R_0805_2012Metric, F.Cu at (70.7, 119.0)
- added R11: 10k, Resistor_SMD:R_0805_2012Metric, F.Cu at (135.9, 53.5)
- added R11: 10k, Resistor_SMD:R_0805_2012Metric, F.Cu at (103.4, 119.0)
- added R11: 10k, Resistor_SMD:R_0805_2012Metric, F.Cu at (70.7, 86.3)
- added R11: 10k, Resistor_SMD:R_0805_2012Metric, F.Cu at (103.3, 53.5)
- added R11: 10k, Resistor_SMD:R_0805_2012Metric, F.Cu at (103.4, 86.3)
- added R11: 10k, Resistor_SMD:R_0805_2012Metric, F.Cu at (136.0, 119.0)
- added R11: 10k, Resistor_SMD:R_0805_2012Metric, F.Cu at (136.0, 86.3)
- added R12: 10k, Resistor_SMD:R_0805_2012Metric, F.Cu at (103.4, 116.5)
- added R12: 10k, Resistor_SMD:R_0805_2012Metric, F.Cu at (135.9, 51.0)
- added R12: 10k, Resistor_SMD:R_0805_2012Metric, F.Cu at (136.0, 116.5)
- added R12: 10k, Resistor_SMD:R_0805_2012Metric, F.Cu at (103.3, 51.0)
- added R12: 10k, Resistor_SMD:R_0805_2012Metric, F.Cu at (70.7, 83.8)
- added R12: 10k, Resistor_SMD:R_0805_2012Metric, F.Cu at (70.7, 116.5)
- added R12: 10k, Resistor_SMD:R_0805_2012Metric, F.Cu at (136.0, 83.8)
- added R12: 10k, Resistor_SMD:R_0805_2012Metric, F.Cu at (103.4, 83.8)
- added R13: 10k, Resistor_SMD:R_0805_2012Metric, F.Cu at (70.7, 114.0)
- added R13: 10k, Resistor_SMD:R_0805_2012Metric, F.Cu at (70.7, 81.3)
- added R13: 10k, Resistor_SMD:R_0805_2012Metric, F.Cu at (136.0, 114.0)
- added R13: 10k, Resistor_SMD:R_0805_2012Metric, F.Cu at (103.3, 48.5)
- added R13: 10k, Resistor_SMD:R_0805_2012Metric, F.Cu at (136.0, 81.3)
- added R13: 10k, Resistor_SMD:R_0805_2012Metric, F.Cu at (135.9, 48.5)
- added R13: 10k, Resistor_SMD:R_0805_2012Metric, F.Cu at (103.4, 81.3)
- added R13: 10k, Resistor_SMD:R_0805_2012Metric, F.Cu at (103.4, 114.0)
- added R14: 10k, Resistor_SMD:R_0805_2012Metric, F.Cu at (135.9, 46.0)
- added R14: 10k, Resistor_SMD:R_0805_2012Metric, F.Cu at (136.0, 78.7)
- added R14: 10k, Resistor_SMD:R_0805_2012Metric, F.Cu at (103.3, 46.0)
- added R14: 10k, Resistor_SMD:R_0805_2012Metric, F.Cu at (70.7, 78.8)
- added R14: 10k, Resistor_SMD:R_0805_2012Metric, F.Cu at (103.4, 78.8)
- added R14: 10k, Resistor_SMD:R_0805_2012Metric, F.Cu at (136.0, 111.5)
- added R14: 10k, Resistor_SMD:R_0805_2012Metric, F.Cu at (103.4, 111.5)
- added R14: 10k, Resistor_SMD:R_0805_2012Metric, F.Cu at (70.7, 111.5)
- added R17: 10k, Resistor_SMD:R_0805_2012Metric, B.Cu at (84.3, 45.6)
- added R17: 10k, Resistor_SMD:R_0805_2012Metric, B.Cu at (51.7, 45.6)
- added R17: 10k, Resistor_SMD:R_0805_2012Metric, B.Cu at (84.4, 111.1)
- added R17: 10k, Resistor_SMD:R_0805_2012Metric, B.Cu at (84.3, 78.3)
- added R17: 10k, Resistor_SMD:R_0805_2012Metric, B.Cu at (116.9, 78.3)
- added R17: 10k, Resistor_SMD:R_0805_2012Metric, B.Cu at (51.7, 111.0)
- added R17: 10k, Resistor_SMD:R_0805_2012Metric, B.Cu at (51.7, 78.3)
- added R17: 10k, Resistor_SMD:R_0805_2012Metric, B.Cu at (116.9, 111.0)
- added R17: 10k, Resistor_SMD:R_0805_2012Metric, B.Cu at (116.9, 45.6)
- added R18: 10k, Resistor_SMD:R_0805_2012Metric, B.Cu at (116.9, 80.8)
- added R18: 10k, Resistor_SMD:R_0805_2012Metric, B.Cu at (116.9, 48.1)
- added R18: 10k, Resistor_SMD:R_0805_2012Metric, B.Cu at (116.9, 113.6)
- added R18: 10k, Resistor_SMD:R_0805_2012Metric, B.Cu at (51.7, 113.6)
- added R18: 10k, Resistor_SMD:R_0805_2012Metric, B.Cu at (84.3, 48.1)
- added R18: 10k, Resistor_SMD:R_0805_2012Metric, B.Cu at (51.7, 48.1)
- added R18: 10k, Resistor_SMD:R_0805_2012Metric, B.Cu at (51.7, 80.8)
- added R18: 10k, Resistor_SMD:R_0805_2012Metric, B.Cu at (84.3, 80.8)
- added R18: 10k, Resistor_SMD:R_0805_2012Metric, B.Cu at (84.4, 113.6)
- added R19: 10k, Resistor_SMD:R_0805_2012Metric, B.Cu at (116.9, 50.6)
- added R19: 10k, Resistor_SMD:R_0805_2012Metric, B.Cu at (51.7, 83.4)
- added R19: 10k, Resistor_SMD:R_0805_2012Metric, B.Cu at (116.9, 116.1)
- added R19: 10k, Resistor_SMD:R_0805_2012Metric, B.Cu at (116.9, 83.4)
- added R19: 10k, Resistor_SMD:R_0805_2012Metric, B.Cu at (51.7, 50.6)
- added R19: 10k, Resistor_SMD:R_0805_2012Metric, B.Cu at (51.7, 116.1)
- added R19: 10k, Resistor_SMD:R_0805_2012Metric, B.Cu at (84.3, 50.6)
- added R19: 10k, Resistor_SMD:R_0805_2012Metric, B.Cu at (84.4, 116.1)
- added R19: 10k, Resistor_SMD:R_0805_2012Metric, B.Cu at (84.3, 83.4)
- added R2: 10k, Resistor_SMD:R_0805_2012Metric, F.Cu at (116.9, 111.0)
- added R2: 10k, Resistor_SMD:R_0805_2012Metric, F.Cu at (84.3, 45.6)
- added R2: 10k, Resistor_SMD:R_0805_2012Metric, F.Cu at (84.4, 111.1)
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- renumbered 5V to 5V1, GND to GND1
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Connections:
- I1 pad 1: +3V3_UP -> Net-(I1-Pad1)
- I10 pad 1: +3V3_UP -> Net-(I10-Pad1)
- I11 pad 1: +3V3_UP -> Net-(I11-Pad1)
- I12 pad 1: +3V3_UP -> Net-(I12-Pad1)
- I2 pad 1: +3V3_UP -> Net-(I2-Pad1)
- I3 pad 1: +3V3_UP -> Net-(I3-Pad1)
- I4 pad 1: +3V3_UP -> Net-(I4-Pad1)
- I5 pad 1: +3V3_UP -> Net-(I5-Pad1)
- I6 pad 1: +3V3_UP -> Net-(I6-Pad1)
- I7 pad 1: +3V3_UP -> Net-(I7-Pad1)
- I8 pad 1: +3V3_UP -> Net-(I8-Pad1)
- I9 pad 1: +3V3_UP -> Net-(I9-Pad1)
- R10 pad 2: +3V3_UP -> Net-(I8-Pad1)
- R11 pad 2: +3V3_UP -> Net-(I9-Pad1)
- R12 pad 2: +3V3_UP -> Net-(I10-Pad1)
- R13 pad 2: +3V3_UP -> Net-(I11-Pad1)
- R14 pad 2: +3V3_UP -> Net-(I12-Pad1)
- R2 pad 2: +3V3_UP -> Net-(I1-Pad1)
- R4 pad 2: +3V3_UP -> Net-(I2-Pad1)
- R5 pad 2: +3V3_UP -> Net-(I3-Pad1)
- R6 pad 2: +3V3_UP -> Net-(I4-Pad1)
- R7 pad 2: +3V3_UP -> Net-(I5-Pad1)
- R8 pad 2: +3V3_UP -> Net-(I6-Pad1)
- R9 pad 2: +3V3_UP -> Net-(I7-Pad1)
- U1 pad 10: /F7 -> /F12
- U1 pad 13: /F8 -> /F11
- U1 pad 14: /F9 -> /F10
- U1 pad 15: /F10 -> /F9
- U1 pad 16: /F11 -> /F8
- U1 pad 17: /F12 -> /F7
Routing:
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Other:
- board size 31.6 x 31.6 mm -> 96.9 x 97.3 mm
